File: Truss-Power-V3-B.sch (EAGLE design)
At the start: 41 parts, among them J1 XF2L-0625-1, U1 TPS61090, U2 MCP73831T-2ACI/OT, U3 MAX17044, U4 SN74LVC1G86DC1LR, U5 SN74LVC1G123, X1 CON-1PIN, X2 MicroB, X3 CON-1PINB, X4 CON-1PIN, X5 CON-1PIN, X6 CON-1PIN

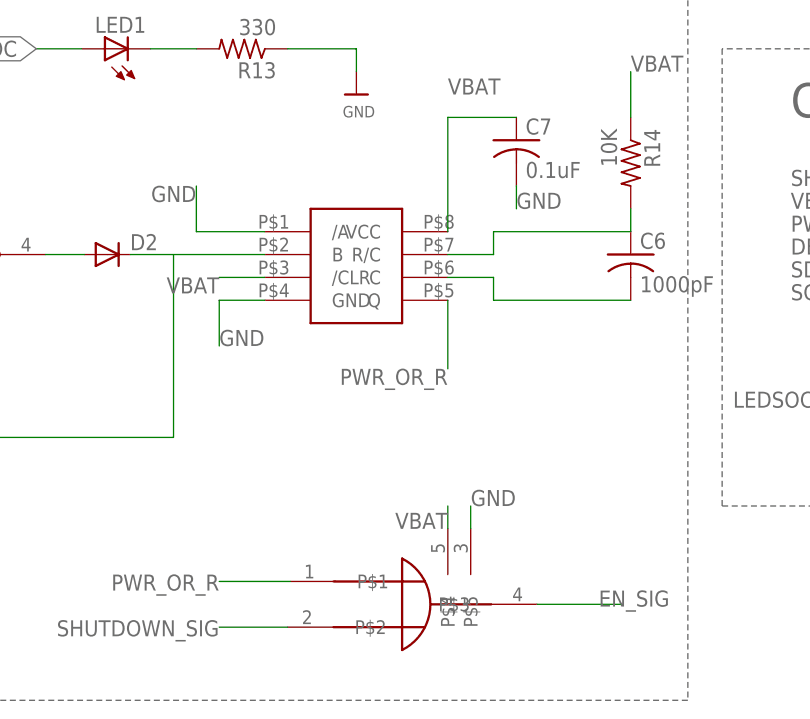
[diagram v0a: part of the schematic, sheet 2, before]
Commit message: Decoupling capacitor added to XOR power supply
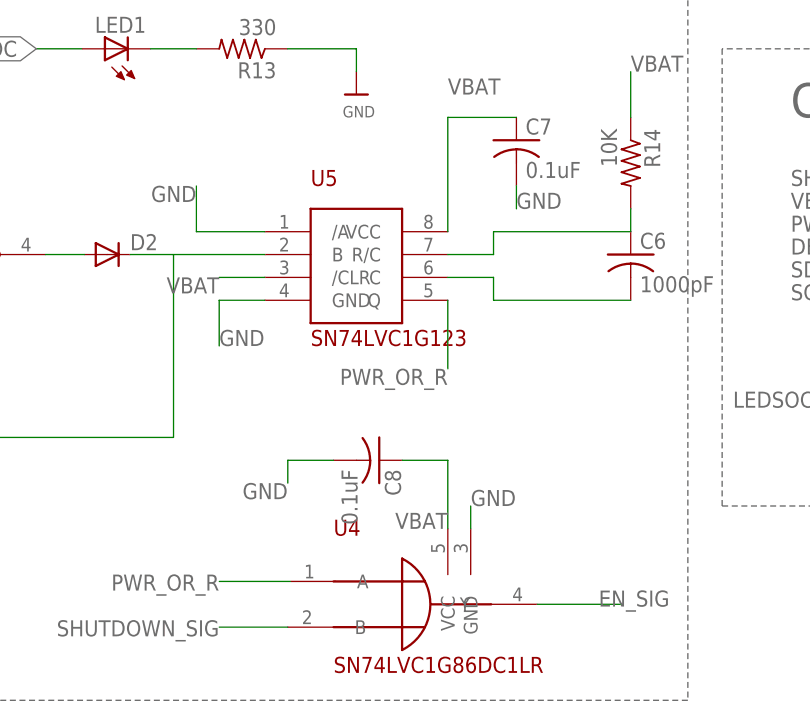
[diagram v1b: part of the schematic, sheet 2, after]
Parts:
- removed R12: 4.7K, resistor:R-US_R0402
- added C8: 0.1uF, rcl:C-USC0603
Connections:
- removed net ALRT: R12.2, U3./ALRT
- net EN_SIG: now also U4.Y; no longer U4.P$3
- net GND: now also C8.2, U4.GND; no longer U4.P$5
- net PWR_OR_R: now also U4.A; no longer U4.P$1
- net SHUTDOWN_SIG: now also U4.B; no longer U4.P$2
- net VBAT: now also C8.1, U4.VCC; no longer U4.P$4
- net VCC: no longer R12.1
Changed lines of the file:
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@@
 <?xml version="1.0" encoding="utf-8"?>
 <!DOCTYPE eagle SYSTEM "eagle.dtd">
-<eagle version="8.4.3">
+<eagle version="8.3.2">
 <drawing>
 <settings>
@@
 <setting verticaltext="up"/>
 </settings>
-<grid distance="0.1" unitdist="inch" unit="inch" style="lines" multiple="1" display="no" altdistance="0.1" altunitdist="inch" altunit="inch"/>
+<grid distance="0.1" unitdist="inch" unit="inch" style="lines" multiple="1" display="no" altdistance="0.01" altunitdist="inch" altunit="inch"/>
 <layers>
 <layer number="1" name="Top" color="4" fill="1" visible="no" active="no"/>
@@
 <part name="U$4" library="microbuilder" deviceset="GND" device=""/>
 <part name="U$19" library="microbuilder" deviceset="GND" device=""/>
-<part name="R12" library="resistor" deviceset="R-US_" device="R0402" value="4.7K"/>
-<part name="P+2" library="supply1" deviceset="VCC" device=""/>
 <part name="C5" library="rcl" deviceset="C-EU" device="C0603" value="1uF"/>
 <part name="U$20" library="microbuilder" deviceset="GND" device=""/>
@@
 <part name="C6" library="rcl" library_urn="urn:adsk.eagle:library:334" deviceset="C-US" device="C0402" package3d_urn="urn:adsk.eagle:package:23626/1" value="1000pF"/>
 <part name="C7" library="rcl" library_urn="urn:adsk.eagle:library:334" deviceset="C-US" device="C0603" package3d_urn="urn:adsk.eagle:package:23616/2" value="0.1uF"/>
+<part name="C8" library="rcl" library_urn="urn:adsk.eagle:library:334" deviceset="C-US" device="C0603" package3d_urn="urn:adsk.eagle:package:23616/2" value="0.1uF"/>
 </parts>
 <sheets>
@@
 <instance part="U$4" gate="G$1" x="38.1" y="33.02"/>
 <instance part="U$19" gate="G$1" x="88.9" y="17.78"/>
-<instance part="R12" gate="G$1" x="104.14" y="15.24" rot="R180"/>
-<instance part="P+2" gate="VCC" x="114.3" y="20.32"/>
 <instance part="C5" gate="G$1" x="40.64" y="27.94"/>
 <instance part="U$20" gate="G$1" x="35.56" y="20.32"/>
@@
 <pinref part="C4" gate="C1" pin="1"/>
 </segment>
-<segment>
-<pinref part="R12" gate="G$1" pin="1"/>
-<pinref part="P+2" gate="VCC" pin="VCC"/>
-<wire x1="109.22" y1="15.24" x2="114.3" y2="15.24" width="0.1524" layer="91"/>
-<wire x1="114.3" y1="15.24" x2="114.3" y2="17.78" width="0.1524" layer="91"/>
-</segment>
 </net>
 <net name="SCL" class="0">
@@
 <wire x1="35.56" y1="17.78" x2="43.18" y2="17.78" width="0.1524" layer="91"/>
 <wire x1="43.18" y1="17.78" x2="43.18" y2="20.32" width="0.1524" layer="91"/>
-</segment>
-</net>
-<net name="ALRT" class="0">
-<segment>
-<pinref part="U3" gate="G$1" pin="/ALRT"/>
-<pinref part="R12" gate="G$1" pin="2"/>
-<wire x1="73.66" y1="15.24" x2="99.06" y2="15.24" width="0.1524" layer="91"/>
 </segment>
 </net>
@@
 <instance part="U$16" gate="G$1" x="20.32" y="53.34"/>
 <instance part="D2" gate="G$1" x="38.354" y="53.34"/>
-<instance part="U4" gate="G$1" x="71.12" y="14.478"/>
+<instance part="U4" gate="U1" x="71.12" y="14.478"/>
 <instance part="X1" gate="G$1" x="185.42" y="55.88"/>
 <instance part="X6" gate="G$1" x="185.42" y="53.34"/>
 <instance part="X3" gate="G$1" x="127" y="38.1"/>
-<instance part="U5" gate="G$1" x="66.04" y="53.34"/>
+<instance part="U5" gate="U1" x="66.04" y="53.34"/>
 <instance part="R14" gate="G$1" x="96.52" y="63.5" rot="R270"/>
 <instance part="C6" gate="G$1" x="96.52" y="53.34"/>
 <instance part="C7" gate="G$1" x="83.82" y="66.04"/>
+<instance part="C8" gate="G$1" x="68.58" y="30.48" rot="R270"/>
 </instances>
 <busses>
@@
 <segment>
 <wire x1="78.74" y1="25.4" x2="78.74" y2="22.86" width="0.1524" layer="91"/>
-<pinref part="U4" gate="G$1" pin="P$5"/>
+<pinref part="U4" gate="U1" pin="GND"/>
 <label x="78.74" y="25.4" size="1.778" layer="95"/>
 </segment>
@@
 </segment>
 <segment>
-<pinref part="U5" gate="G$1" pin="/A"/>
+<pinref part="U5" gate="U1" pin="/A"/>
 <wire x1="55.88" y1="55.88" x2="48.26" y2="55.88" width="0.1524" layer="91"/>
 <wire x1="48.26" y1="55.88" x2="48.26" y2="60.96" width="0.1524" layer="91"/>
@@
 </segment>
 <segment>
-<pinref part="U5" gate="G$1" pin="GND"/>
+<pinref part="U5" gate="U1" pin="GND"/>
 <wire x1="55.88" y1="48.26" x2="50.8" y2="48.26" width="0.1524" layer="91"/>
 <wire x1="50.8" y1="48.26" x2="50.8" y2="43.18" width="0.1524" layer="91"/>
@@
 <label x="83.82" y="58.42" size="1.778" layer="95"/>
 </segment>
+<segment>
+<pinref part="C8" gate="G$1" pin="2"/>
+<wire x1="63.5" y1="30.48" x2="58.42" y2="30.48" width="0.1524" layer="91"/>
+<wire x1="58.42" y1="30.48" x2="58.42" y2="27.94" width="0.1524" layer="91"/>
+<label x="58.42" y="27.94" size="1.778" layer="95" rot="R180"/>
+</segment>
 </net>
 <net name="VBAT" class="0">
@@
 </segment>
 <segment>
-<pinref part="U4" gate="G$1" pin="P$4"/>
-<wire x1="76.2" y1="22.86" x2="76.2" y2="25.4" width="0.1524" layer="91"/>
+<pinref part="U4" gate="U1" pin="VCC"/>
 <label x="76.2" y="24.638" size="1.778" layer="95" rot="R180"/>
-</segment>
-<segment>
-<pinref part="U5" gate="G$1" pin="VCC"/>
+<wire x1="76.2" y1="22.86" x2="76.2" y2="30.48" width="0.1524" layer="91"/>
+<pinref part="C8" gate="G$1" pin="1"/>
+<wire x1="76.2" y1="30.48" x2="71.12" y2="30.48" width="0.1524" layer="91"/>
+</segment>
+<segment>
+<pinref part="U5" gate="U1" pin="VCC"/>
 <wire x1="76.2" y1="55.88" x2="76.2" y2="68.58" width="0.1524" layer="91"/>
 <label x="76.2" y="71.12" size="1.778" layer="95"/>
@@
 </segment>
 <segment>
-<pinref part="U5" gate="G$1" pin="/CLR"/>
+<pinref part="U5" gate="U1" pin="/CLR"/>
 <wire x1="55.88" y1="50.8" x2="50.8" y2="50.8" width="0.1524" layer="91"/>
 <label x="50.8" y="50.8" size="1.778" layer="95" rot="R180"/>
@@
 <net name="EN_SIG" class="0">
 <segment>
-<pinref part="U4" gate="G$1" pin="P$3"/>
+<pinref part="U4" gate="U1" pin="Y"/>
 <wire x1="86.106" y1="14.478" x2="95.504" y2="14.478" width="0.1524" layer="91"/>
 <label x="92.964" y="14.224" size="1.778" layer="95"/>
@@
 </segment>
 <segment>
-<pinref part="U4" gate="G$1" pin="P$2"/>
+<pinref part="U4" gate="U1" pin="B"/>
 <wire x1="58.42" y1="11.938" x2="50.8" y2="11.938" width="0.1524" layer="91"/>
 <label x="50.8" y="12.7" size="1.778" layer="95" rot="R180"/>
@@
 <wire x1="17.78" y1="33.02" x2="45.72" y2="33.02" width="0.1524" layer="91"/>
 <wire x1="45.72" y1="33.02" x2="45.72" y2="53.34" width="0.1524" layer="91"/>
-<pinref part="U5" gate="G$1" pin="B"/>
+<pinref part="U5" gate="U1" pin="B"/>
 <wire x1="45.72" y1="53.34" x2="55.88" y2="53.34" width="0.1524" layer="91"/>
 </segment>
@@
 <net name="PWR_OR_R" class="0">
 <segment>
-<pinref part="U5" gate="G$1" pin="Q"/>
+<pinref part="U5" gate="U1" pin="Q"/>
 <wire x1="76.2" y1="48.26" x2="76.2" y2="40.64" width="0.1524" layer="91"/>
 <label x="76.2" y="40.64" size="1.778" layer="95" rot="R180"/>
 </segment>
 <segment>
-<pinref part="U4" gate="G$1" pin="P$1"/>
+<pinref part="U4" gate="U1" pin="A"/>
 <wire x1="58.674" y1="17.018" x2="50.8" y2="17.018" width="0.1524" layer="91"/>
 <label x="50.8" y="17.78" size="1.778" layer="95" rot="R180"/>
@@
 <net name="N$8" class="0">
 <segment>
-<pinref part="U5" gate="G$1" pin="R/C"/>
+<pinref part="U5" gate="U1" pin="R/C"/>
 <wire x1="76.2" y1="53.34" x2="81.28" y2="53.34" width="0.1524" layer="91"/>
 <wire x1="81.28" y1="53.34" x2="81.28" y2="55.88" width="0.1524" layer="91"/>
@@
 <net name="N$10" class="0">
 <segment>
-<pinref part="U5" gate="G$1" pin="C"/>
+<pinref part="U5" gate="U1" pin="C"/>
 <wire x1="76.2" y1="50.8" x2="81.28" y2="50.8" width="0.1524" layer="91"/>
 <wire x1="81.28" y1="50.8" x2="81.28" y2="48.26" width="0.1524" layer="91"/>

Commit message: Final board files
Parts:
- R13: value 330 -> 1K
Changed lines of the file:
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@@
 <?xml version="1.0" encoding="utf-8"?>
 <!DOCTYPE eagle SYSTEM "eagle.dtd">
-<eagle version="8.3.2">
+<eagle version="8.4.3">
 <drawing>
 <settings>
@@
 <part name="U$21" library="microbuilder" deviceset="VBAT" device=""/>
 <part name="LED1" library="led" library_urn="urn:adsk.eagle:library:259" deviceset="LED" device="CHIP-LED0603" package3d_urn="urn:adsk.eagle:package:15819/1"/>
-<part name="R13" library="resistor" deviceset="R-US_" device="R0402" value="330"/>
+<part name="R13" library="resistor" deviceset="R-US_" device="R0402" value="1K"/>
 <part name="U$22" library="microbuilder" deviceset="GND" device=""/>
 <part name="R7" library="resistor" deviceset="R-US_" device="R0402" value="470"/>
